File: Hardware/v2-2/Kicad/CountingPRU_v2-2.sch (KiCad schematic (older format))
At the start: 47 parts, among them J1 BBB, J2 IN_ETHERNET, J3 BERGOZ_02, J4 BERGOZ_01, P1 LNLS, Q1 BSR14, Q2 BSR14, Q3 BSR14, T2 Transformer_1P_1S, T3 Transformer_1P_1S, U1 741G74, U10 1G125, U11 1G125, U12 1G04, U13 1G04, U14 TS5A21366, U15 TS5A21366, U2 741G74, U3 741G74, U4 741G74, U5 741G74, U6 741G74, U7 1G04, U8 1G125, U9 1G125

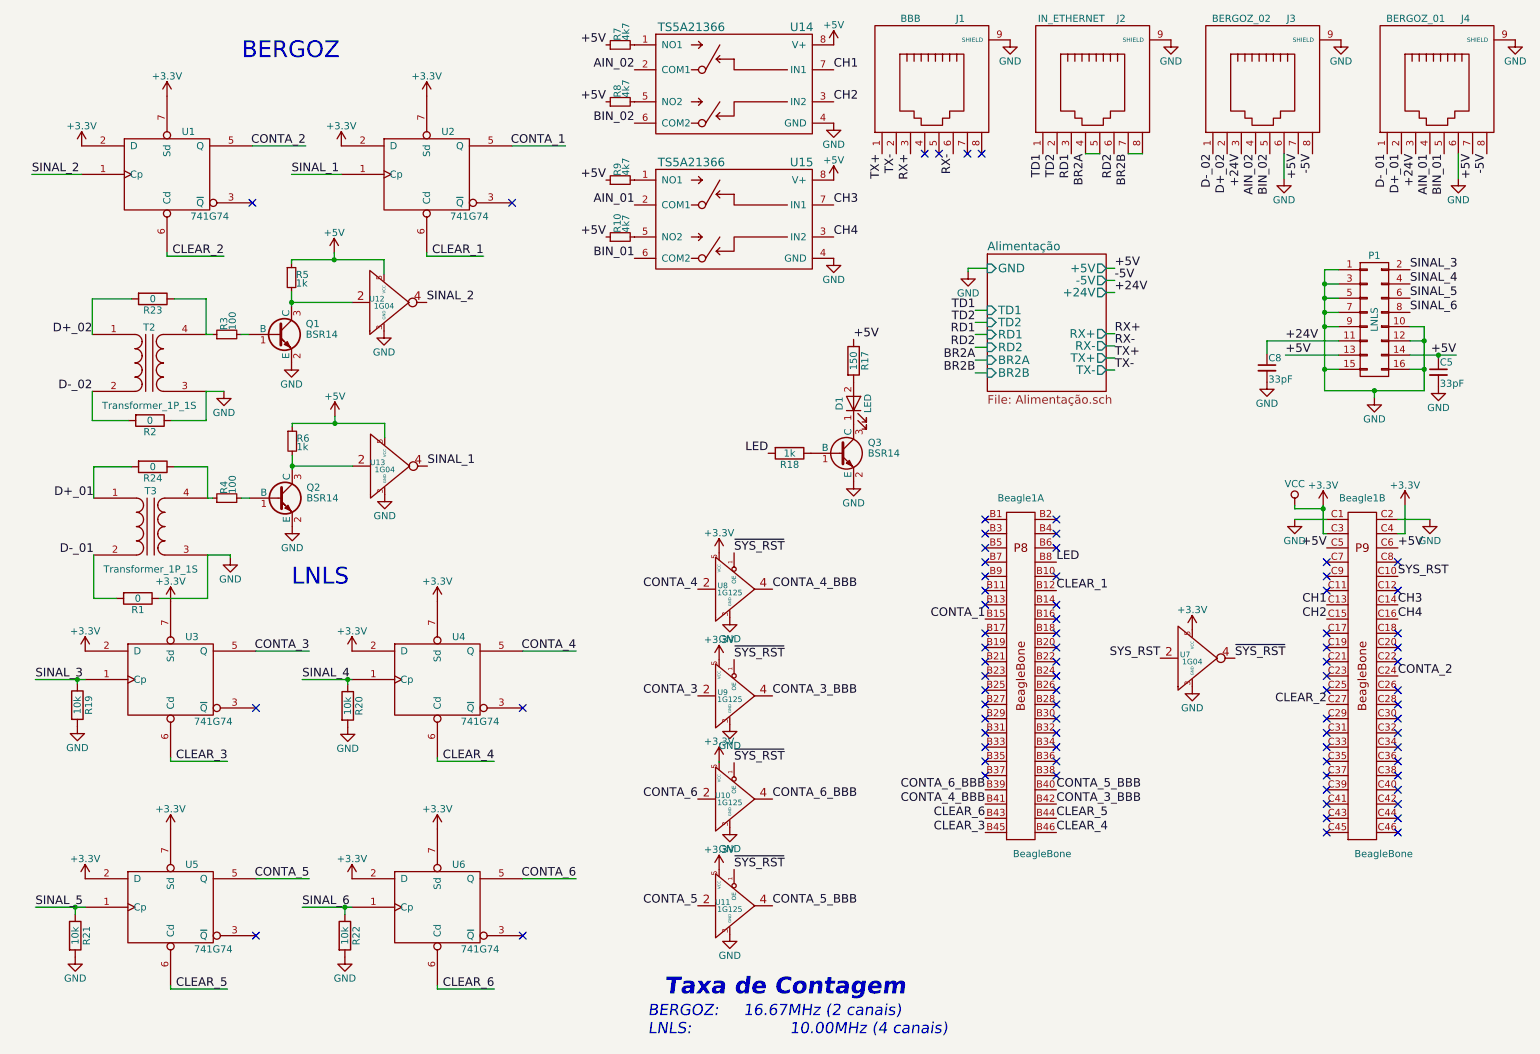
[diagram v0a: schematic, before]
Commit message: Updating files for 2 LNLS connector
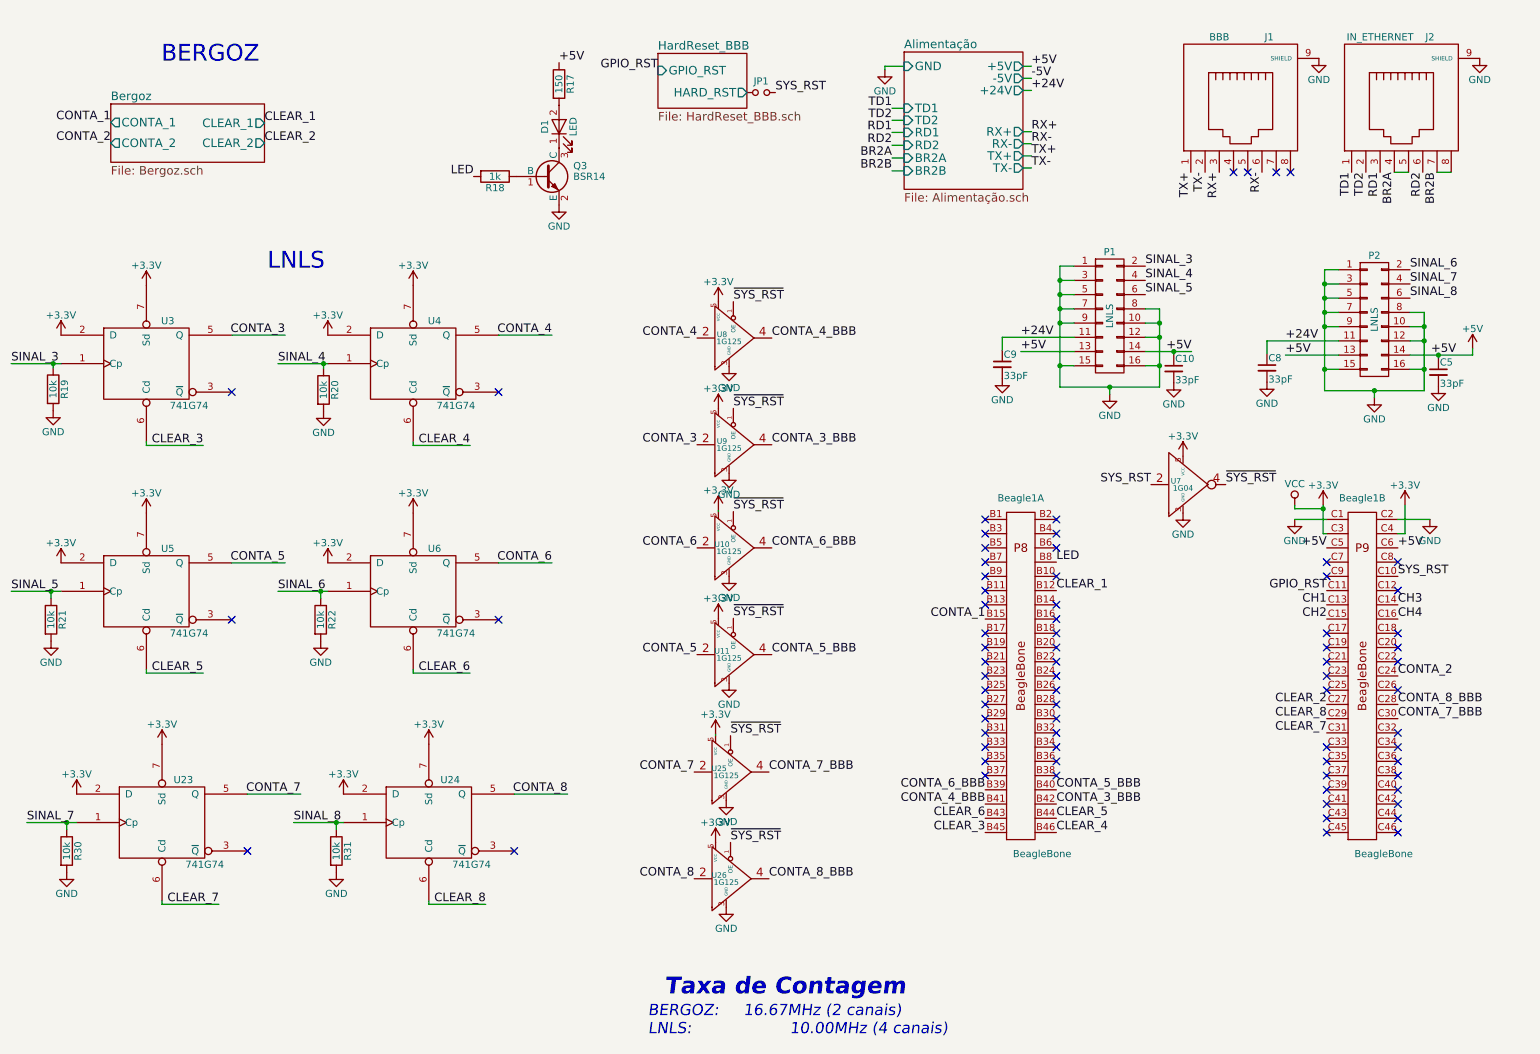
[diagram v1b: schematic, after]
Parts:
- removed J3: BERGOZ_02, Controle:RJ45-STEWART, symbol RJ45
- removed J4: BERGOZ_01, Controle:RJ45-STEWART, symbol RJ45
- removed Q1, Q2: BSR14, TO_SOT_Packages_SMD:SOT-23_Handsoldering, symbol 2SC1945
- removed R1, R2, R23, R24: 0, Resistors_SMD:R_0805, symbol R
- removed R10, R7, R8, R9: 4k7, Resistors_SMD:R_0805, symbol R_Small
- removed R3, R4: 100, Resistors_SMD:R_0805, symbol R_Small
- removed R5, R6: 1k, Resistors_SMD:R_0805, symbol R_Small
- removed T2, T3: Transformer_1P_1S, Controle:Trafo_murata_SMD, symbol Transformer_1P_1S
- removed U1, U2: 741G74, CONTROLE:TSSOP-8, symbol 741G74
- removed U12, U13: 1G04, TO_SOT_Packages_SMD:SOT-353_SC-70-5_Handsoldering, symbol 1G04
- removed U14, U15: TS5A21366, Controle:VSSOP-8, symbol TS5A21366
- added C10, C9: 33pF, Capacitors_SMD:C_0805, symbol C_Small
- added JP1: HR, Pin_Headers:Pin_Header_Straight_1x02_Pitch2.54mm, symbol Jumper_NO_Small
- added P1: LNLS, Pin_Headers:Pin_Header_Angled_2x08_Pitch1.27mm, symbol CONN_02X08
- added R30, R31: 10k, Resistors_SMD:R_0805, symbol R
- added U23, U24: 741G74, CONTROLE:TSSOP-8, symbol 741G74
- added U25, U26: 1G125, TO_SOT_Packages_SMD:SOT-353_SC-70-5_Handsoldering, symbol 1G125
- renumbered P1 to P2
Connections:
- net +24V: now also C9.1, P1.11 (P11)
- net +3V3: now also U23.2 (D), U23.7 (Sd), U23.8 (VCC), U24.2 (D), U24.7 (Sd), U24.8 (VCC), U25.5 (VCC), U26.5 (VCC)
- net +5V: now also C10.1, P1.13 (P13), P1.14 (P14)
- net GND: now also P2.8 (P8), C10.2, C9.2, P1.1 (P1), P1.10 (P10), P1.12 (P12), P1.15 (P15), P1.16 (P16), P1.3 (P3), P1.5 (P5), P1.7 (P7), P1.8 (P8), P1.9 (P9), R30.2, R31.2, U23.4 (GND), U24.4 (GND), U25.3 (GND), U26.3 (GND)
- net SINAL_3: now also P1.2 (P2); no longer P2.2 (P2)
- net SINAL_4: now also P1.4 (P4); no longer P2.4 (P4)
- net SINAL_5: now also P1.6 (P6); no longer P2.6 (P6)
- net SINAL_6: now also P2.2 (P2); no longer P2.8 (P8)
- net SYS_RST: now also JP1.2
- net ~SYS_RST: now also U25.1 (OE), U26.1 (OE)
- net GPIO_RST: now reaches Beagle1.C11
- net CONTA_8_BBB: now reaches Beagle1.C28
- net CONTA_8_BBB: now also U26.4
- net CLEAR_8: now reaches Beagle1.C29
- net CLEAR_8: now also U24.6 (Cd)
- net CONTA_7_BBB: now reaches Beagle1.C30
- net CONTA_7_BBB: now also U25.4
- net CLEAR_7: now reaches Beagle1.C31
- net CLEAR_7: now also U23.6 (Cd)
- new net CONTA_7: U23.5 (Q), U25.2
- new net CONTA_8: U24.5 (Q), U26.2
- new net HardReset_BBB/HARD_RST: JP1.1
- new net SINAL_7: P2.4 (P4), R30.1, U23.1 (Cp)
- new net SINAL_8: P2.6 (P6), R31.1, U24.1 (Cp)
- no-connect marks 78 -> 73
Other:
- moved on the sheet: D1, J1, J2, Q3, R17, R18, R19, R20, R21, R22, U10, U11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

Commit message: Update
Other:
- note added: "1 canal: 14.29MHz | 3 canais: 11.11MHz\n2 canais: 12.50MHz | 4 canais: 10.00MHz"
- note added: "Taxa Máxima de Contagem\nCanais conectados por PRU"
- note removed: "BERGOZ: 16.67MHz (2 canais)\nLNLS: 10.00MHz (4 canais)"
- note removed: "Taxa de Contagem"
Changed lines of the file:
@@
 Text Label 7375 6275 2    60   ~ 0
 CLEAR_3
-Text Notes 5005 7705 0    79   Italic 0
-BERGOZ: 	16.67MHz (2 canais)\nLNLS:					10.00MHz (4 canais)
-Text Notes 5120 7430 0    118  Italic 24
-Taxa de Contagem
+Text Notes 4245 7725 0    79   Italic 0
+1 canal: 	14.29MHz		|	3 canais:	11.11MHz\n2 canais:	12.50MHz		|	4 canais:	10.00MHz
+Text Notes 4310 7415 0    118  Italic 24
+Taxa Máxima de Contagem\nCanais conectados por PRU
 Text Label 10275 4475 0    60   ~ 0
 SYS_RST

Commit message: Update hardware files
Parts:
- R17: value 150 -> 180
